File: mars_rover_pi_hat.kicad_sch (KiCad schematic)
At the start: 11 parts, among them J1 Raspberry_Pi_4, J2 Conn_01x03, J3 Conn_01x03, J4 Conn_01x04, J5 Conn_01x04, J6 Conn_01x03, J7 Conn_01x04, J8 Conn_01x04

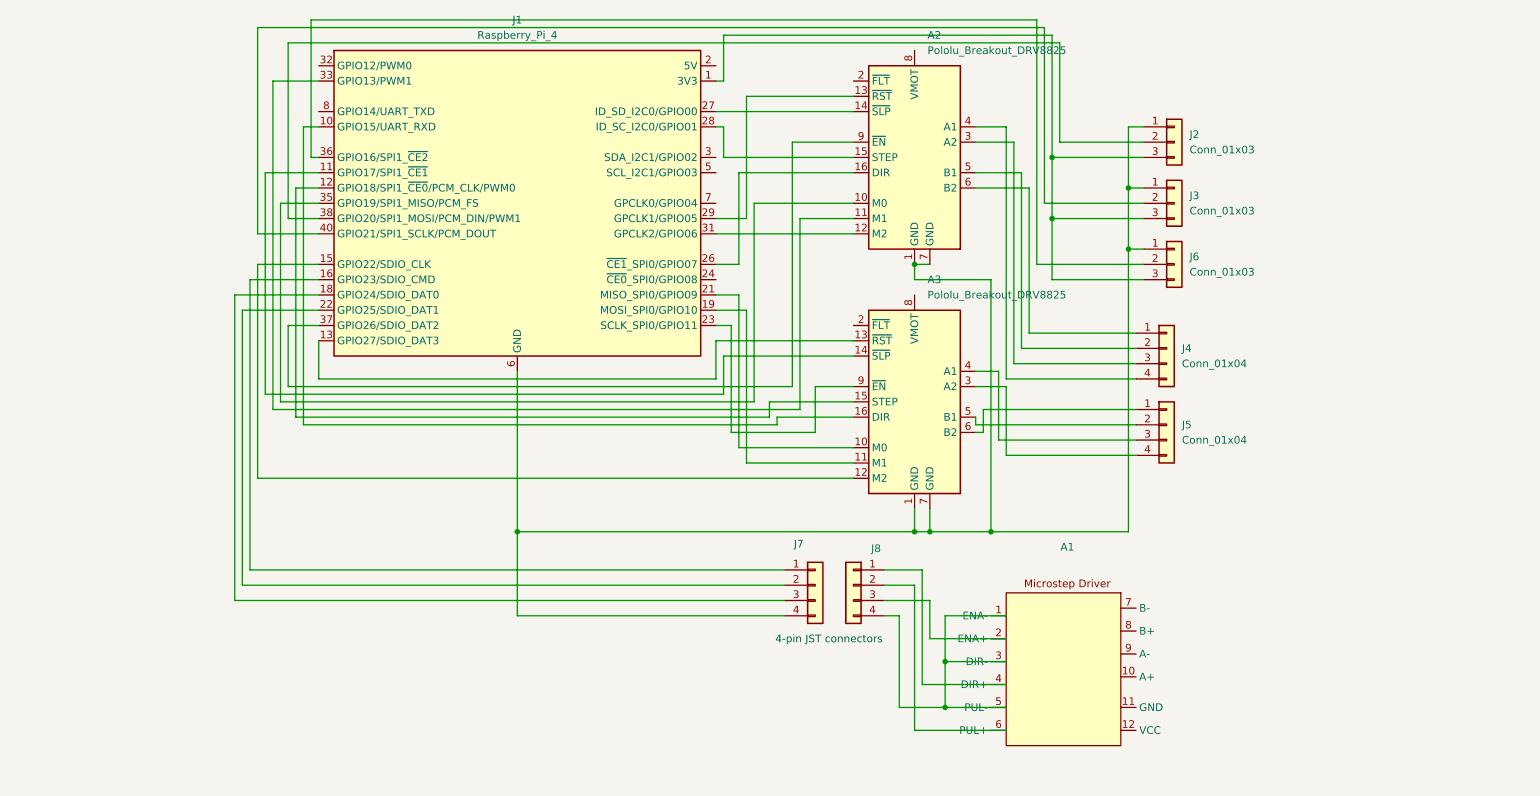
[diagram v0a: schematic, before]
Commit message: added IC for DRV8825
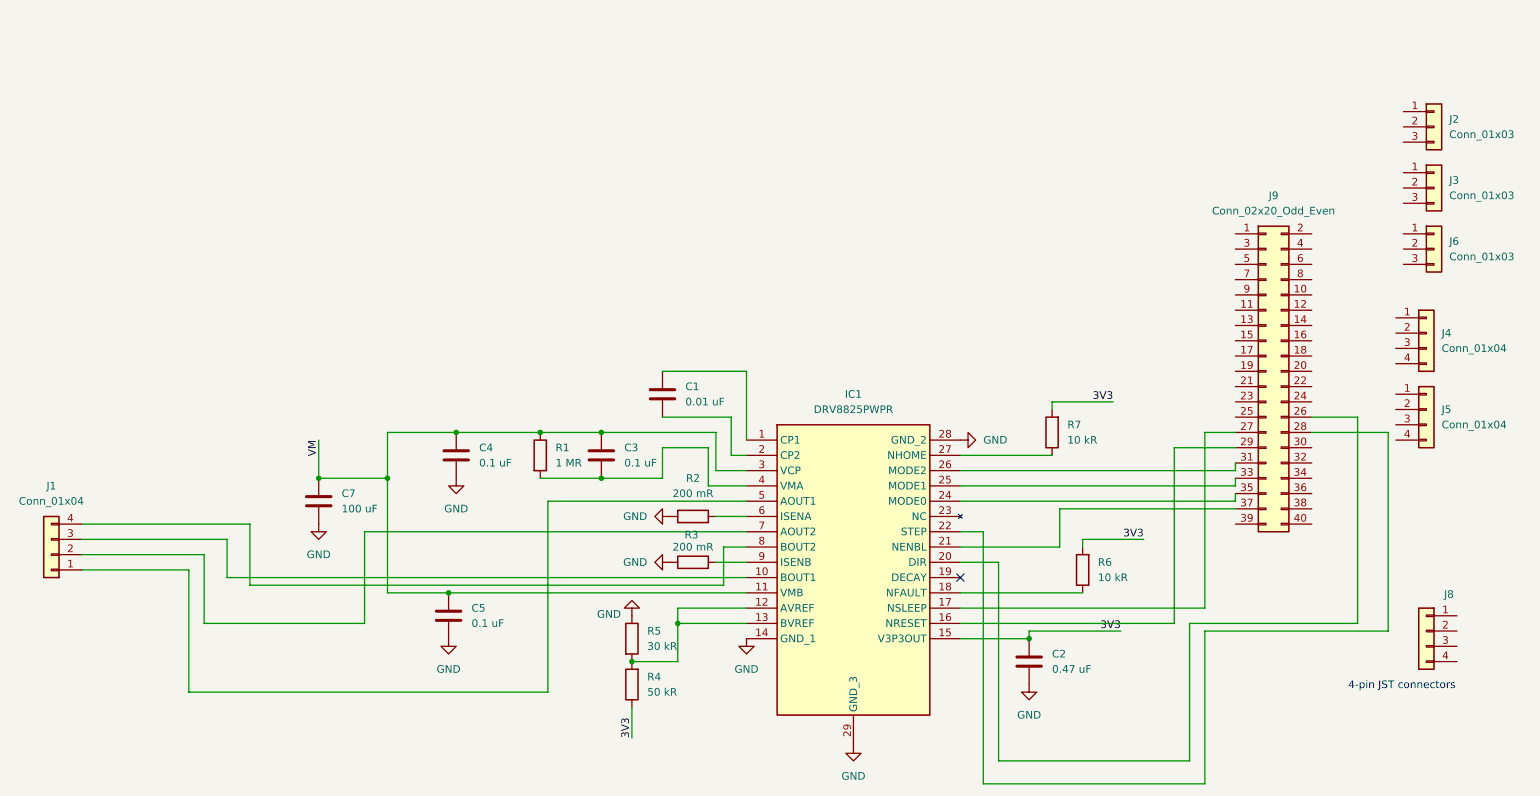
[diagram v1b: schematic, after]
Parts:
- removed A1: ~, symbol MyModules:TB6600_Driver
- removed A2, A3: Pololu_Breakout_DRV8825, Module:Pololu_Breakout-16_15.2x20.3mm, symbol Driver_Motor:Pololu_Breakout_DRV8825
- removed J1: Raspberry_Pi_4, symbol Connector:Raspberry_Pi_4
- removed J7: Conn_01x04, symbol Connector_Generic:Conn_01x04
- added C1: 0.01 uF, symbol Device:C
- added C2: 0.47 uF, symbol Device:C
- added C3, C4, C5: 0.1 uF, symbol Device:C
- added C7: 100 uF, symbol Device:C
- added IC1: DRV8825PWPR, SOP65P640X120-29N, symbol pi_hat:DRV8825PWPR
- added J1: Conn_01x04, symbol Connector_Generic:Conn_01x04
- added J9: Conn_02x20_Odd_Even, symbol Connector_Generic:Conn_02x20_Odd_Even
- added R1: 1 MR, symbol Device:R
- added R2, R3: 200 mR, symbol Device:R
- added R4: 50 kR, symbol Device:R
- added R5: 30 kR, symbol Device:R
- added R6, R7: 10 kR, symbol Device:R
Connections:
- new net: IC1.18 (NFAULT), R6.1
- new net: C1.1, IC1.1 (CP1)
- new net: C1.2, IC1.2 (CP2)
- new net: IC1.12 (AVREF), IC1.13 (BVREF), R4.2, R5.2
- new net: IC1.20 (DIR), J9.26 (Pin_26)
- new net: IC1.17 (NSLEEP), J9.27 (Pin_27)
- new net: IC1.22 (STEP), J9.28 (Pin_28)
- new net: IC1.16 (NRESET), J9.29 (Pin_29)
- new net: IC1.26 (MODE2), J9.31 (Pin_31)
- new net: IC1.25 (MODE1), J9.33 (Pin_33)
- new net: IC1.24 (MODE0), J9.35 (Pin_35)
- new net: IC1.21 (NENBL), J9.37 (Pin_37)
- new net: IC1.10 (BOUT1), J1.3 (Pin_3)
- new net: IC1.27 (NHOME), R7.1
- new net: C3.1, IC1.4 (VMA), R1.2
- new net: IC1.5 (AOUT1), J1.1 (Pin_1)
- new net: IC1.6 (ISENA), R2.2
- new net: IC1.7 (AOUT2), J1.2 (Pin_2)
- new net: IC1.8 (BOUT2), J1.4 (Pin_4)
- new net: IC1.9 (ISENB), R3.2
- new net 3V3: C2.1, IC1.15 (V3P3OUT), R4.1, R6.2, R7.2
- new net GND: C2.2, C4.2, C5.2, C7.2, IC1.14 (GND_1), IC1.28 (GND_2), IC1.29 (GND_3), R2.1, R3.1, R5.1
- new net VM: C3.2, C4.1, C5.1, C7.1, IC1.11 (VMB), IC1.3 (VCP), R1.1
- now unconnected: J2.1 (Pin_1), J2.3 (Pin_3), J3.1 (Pin_1), J3.3 (Pin_3), J6.1 (Pin_1), J6.3 (Pin_3)
- no-connect marks 0 -> 1
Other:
- moved on the sheet: J2, J3, J4, J5, J6, J8
